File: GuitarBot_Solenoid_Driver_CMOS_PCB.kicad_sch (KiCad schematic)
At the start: 37 parts, among them J1 Screw_Terminal_01x02, J10 Screw_Terminal_01x02, J11 Screw_Terminal_01x02, J12 Screw_Terminal_01x02, J13 Screw_Terminal_01x02, J14 Screw_Terminal_01x02, J15 Screw_Terminal_01x02, J16 Screw_Terminal_01x02, J17 Screw_Terminal_01x04, J18 Screw_Terminal_01x02, J2 Screw_Terminal_01x02, J3 Screw_Terminal_01x02, J4 Screw_Terminal_01x02, J5 Screw_Terminal_01x02, J6 Screw_Terminal_01x02, J7 Screw_Terminal_01x02, J8 Screw_Terminal_01x02, J9 Screw_Terminal_01x02, Q1 NMOS, Q2 NMOS, Q3 NMOS, Q4 NMOS, Q5 PMOS, Q6 PMOS, Q7 PMOS, Q8 PMOS, U1 MCP23008-xSO

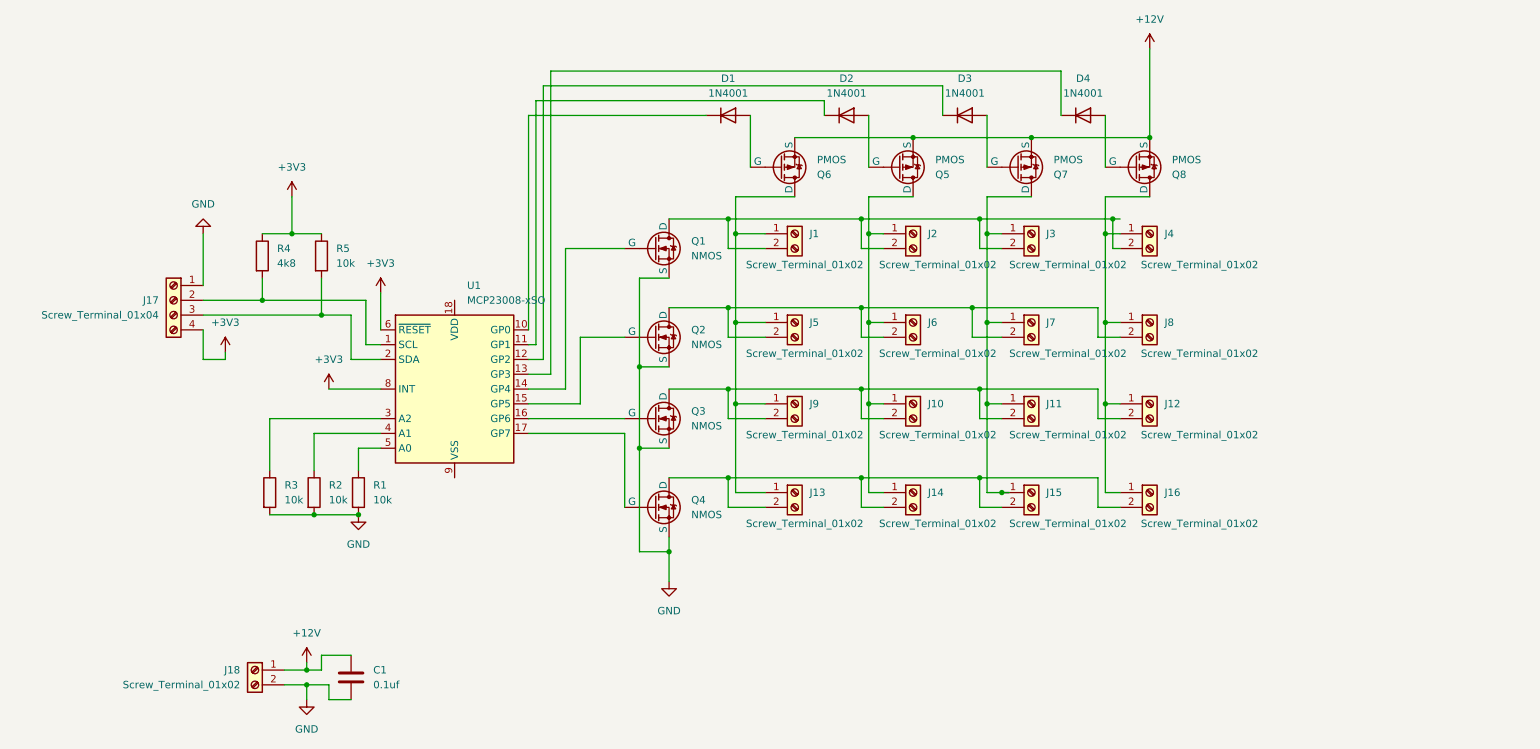
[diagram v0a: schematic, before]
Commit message: cmos schematic footprints
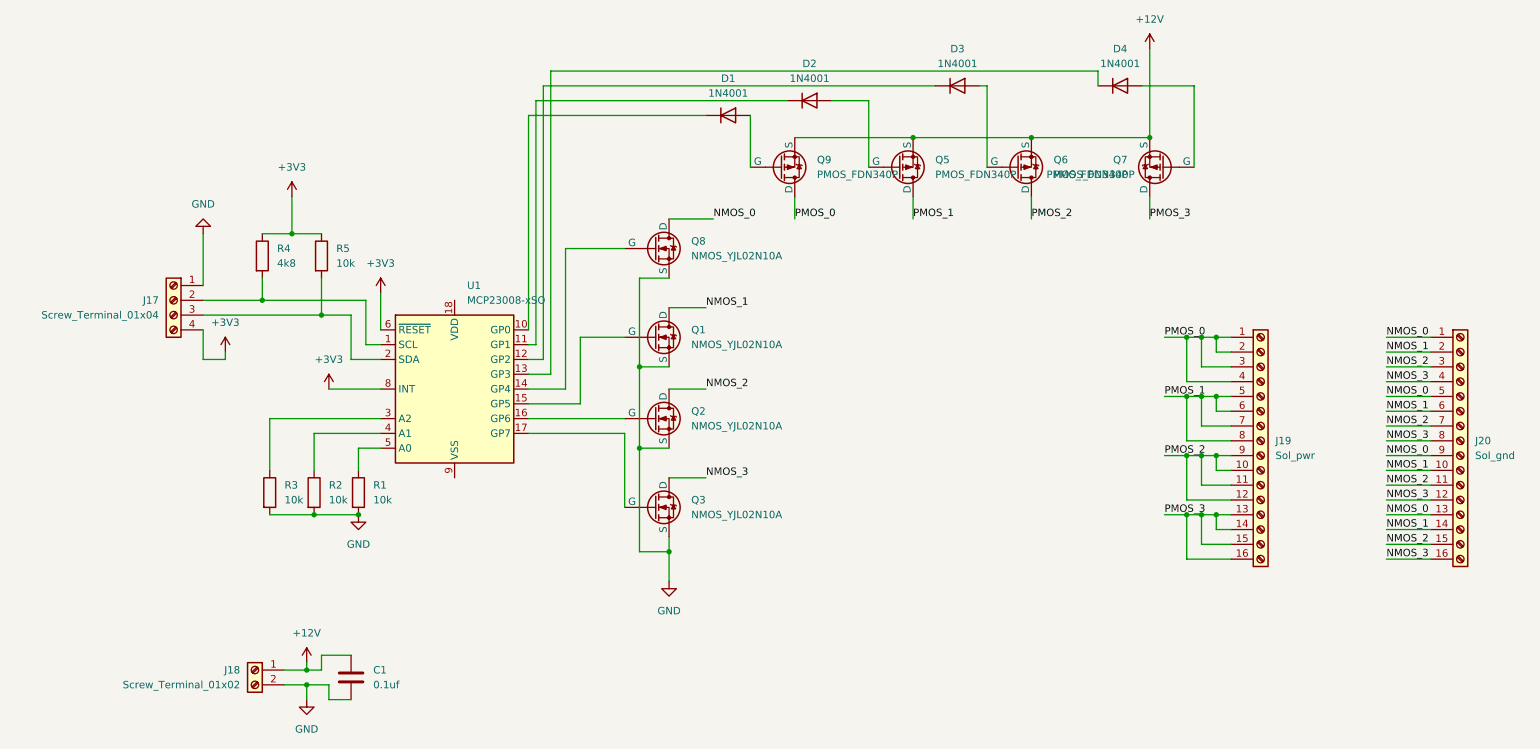
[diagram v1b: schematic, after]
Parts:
- removed J1, J10, J11, J12, J13, J14, J15, J16, J2, J3, J4, J5, J6, J7, J8, J9: Screw_Terminal_01x02, symbol Connector:Screw_Terminal_01x02
- removed Q1, Q2, Q3, Q4: NMOS, symbol Simulation_SPICE:NMOS
- removed Q5, Q6, Q7, Q8: PMOS, symbol Simulation_SPICE:PMOS
- added J19: Sol_pwr, Connector_PinSocket_2.54mm:PinSocket_1x16_P2.54mm_Vertical, symbol Connector:Screw_Terminal_01x16
- added J20: Sol_gnd, Connector_PinSocket_2.54mm:PinSocket_1x16_P2.54mm_Vertical, symbol Connector:Screw_Terminal_01x16
- added Q1, Q2, Q3, Q8: NMOS_YJL02N10A, Package_TO_SOT_SMD:SOT-23, symbol NURC Custom symbols:NMOS_YJL02N10A
- added Q5, Q6, Q7, Q9: PMOS_FDN340P, Package_TO_SOT_SMD:SOT-23, symbol NURC_Custom_Symbols:PMOS_FDN340P
- C1: footprint (none) -> Capacitor_SMD:C_0402_1005Metric
- J17: footprint (none) -> Connector_PinSocket_2.54mm:PinSocket_1x04_P2.54mm_Vertical
- J18: footprint (none) -> Connector_Phoenix_MSTB:PhoenixContact_MSTBA_2,5_2-G_1x02_P5.00mm_Horizontal
- R1, R2, R3, R4, R5: footprint (none) -> Resistor_SMD:R_1206_3216Metric
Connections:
- net +12V: now also Q5.2 (S), Q6.2 (S), Q7.2 (S), Q9.2 (S)
- net GND: now also Q1.2 (S), Q2.2 (S), Q3.2 (S), Q8.2 (S)
- net at D1.2 (A): now also Q9.1 (G)
- net at D4.2 (A): now also Q7.1 (G)
- net at D3.2 (A): now also Q6.1 (G)
- net at U1.15 (GP5): now also Q1.1 (G)
- net at D2.2 (A): now also Q5.1 (G)
- net at U1.17 (GP7): now also Q3.1 (G)
- net at U1.14 (GP4): now also Q8.1 (G)
- net at U1.16 (GP6): now also Q2.1 (G)
- new net NMOS_0: J20.1 (Pin_1), J20.13 (Pin_13), J20.5 (Pin_5), J20.9 (Pin_9), Q8.3 (D)
- new net NMOS_1: J20.10 (Pin_10), J20.14 (Pin_14), J20.2 (Pin_2), J20.6 (Pin_6), Q1.3 (D)
- new net NMOS_2: J20.11 (Pin_11), J20.15 (Pin_15), J20.3 (Pin_3), J20.7 (Pin_7), Q2.3 (D)
- new net NMOS_3: J20.12 (Pin_12), J20.16 (Pin_16), J20.4 (Pin_4), J20.8 (Pin_8), Q3.3 (D)
- new net PMOS_0: J19.1 (Pin_1), J19.2 (Pin_2), J19.3 (Pin_3), J19.4 (Pin_4), Q9.3 (D)
- new net PMOS_1: J19.5 (Pin_5), J19.6 (Pin_6), J19.7 (Pin_7), J19.8 (Pin_8), Q5.3 (D)
- new net PMOS_2: J19.10 (Pin_10), J19.11 (Pin_11), J19.12 (Pin_12), J19.9 (Pin_9), Q6.3 (D)
- new net PMOS_3: J19.13 (Pin_13), J19.14 (Pin_14), J19.15 (Pin_15), J19.16 (Pin_16), Q7.3 (D)
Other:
- moved on the sheet: D2, D3, D4

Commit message: Modified ./old schematic to use NMOS instead of Darlington transistor array
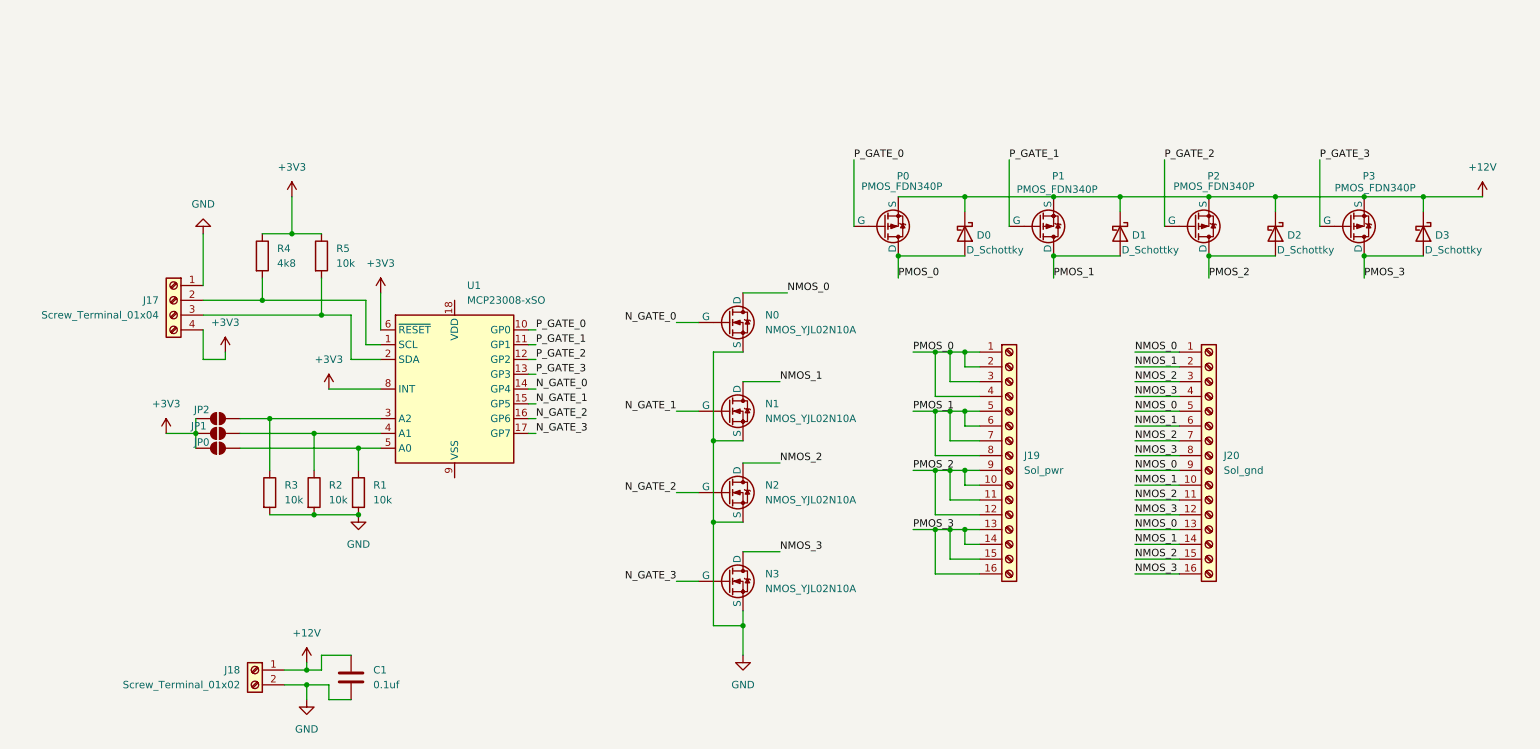
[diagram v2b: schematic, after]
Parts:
- removed D1, D2, D3, D4: 1N4001, Diode_THT:D_DO-41_SOD81_P10.16mm_Horizontal, symbol Diode:1N4001
- added D0, D1, D2, D3: D_Schottky, symbol Device:D_Schottky
- added JP0, JP1, JP2: SolderJumper_2_Open, Jumper:SolderJumper-2_P1.3mm_Open_Pad1.0x1.5mm, symbol Jumper:SolderJumper_2_Open
- renumbered Q8 to N0, Q1 to N1, Q2 to N2, Q3 to N3, Q9 to P0, Q5 to P1, Q6 to P2, Q7 to P3
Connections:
- net +12V: now also D0.1 (K), D1.1 (K), D2.1 (K), D3.1 (K)
- net +3V3: now also JP0.1 (A), JP1.1 (A), JP2.1 (A)
- net PMOS_0: now also D0.2 (A)
- net PMOS_1: now also D1.2 (A)
- net PMOS_2: now also D2.2 (A)
- net PMOS_3: now also D3.2 (A)
- net P_GATE_3: now reaches P3.1 (G)
- net P_GATE_3: now also U1.13 (GP3)
- net P_GATE_0: now reaches U1.10 (GP0)
- net P_GATE_0: now also P0.1 (G)
- net N_GATE_2: now reaches N2.1 (G), U1.16 (GP6)
- net P_GATE_2: now reaches U1.12 (GP2)
- net P_GATE_2: now also P2.1 (G)
- net N_GATE_0: now reaches N0.1 (G), U1.14 (GP4)
- net at R1.1, U1.5 (A0): now also JP0.2 (B)
- net at R3.1, U1.3 (A2): now also JP2.2 (B)
- net N_GATE_1: now reaches N1.1 (G), U1.15 (GP5)
- net P_GATE_1: now reaches U1.11 (GP1)
- net P_GATE_1: now also P1.1 (G)
- net N_GATE_3: now reaches N3.1 (G), U1.17 (GP7)
- net at R2.1, U1.4 (A1): now also JP1.2 (B)
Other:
- moved on the sheet: J19, J20, N0, N1, N2, N3, P0, P1, P2, P3
